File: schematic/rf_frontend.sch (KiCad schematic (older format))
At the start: 75 parts, among them J9 CONN_01X02, U10 Anaren_B0430J50100AHF, U11 MurataSF2314E, U12 MurataSF2314E, U13 SPF5043Z, U14 RFPA0133TR7, U15 MurataSF2314E, U16 RFSW1012, U17 MurataSF2314E, U8 SX1257, U9 SX1257

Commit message: Updates to schematic, components
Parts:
- C38, C45, C46, C47, C48, C49, C50, C51, C52, C53, C54, C55, C56, C57, C58, C60, C61, C62: footprint (none) -> Capacitors_SMD:C_0402
- C39, C40, C41, C42: value C -> 100nF; footprint (none) -> Capacitors_SMD:C_0402
- C43, C44: value C -> 10nF; footprint (none) -> Capacitors_SMD:C_0402
- C59, C66, C67: footprint 0603 -> Capacitors_SMD:C_0603
- C80: renamed from 1nF1; value C -> 100nF
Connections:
- wire segments 248 -> 249

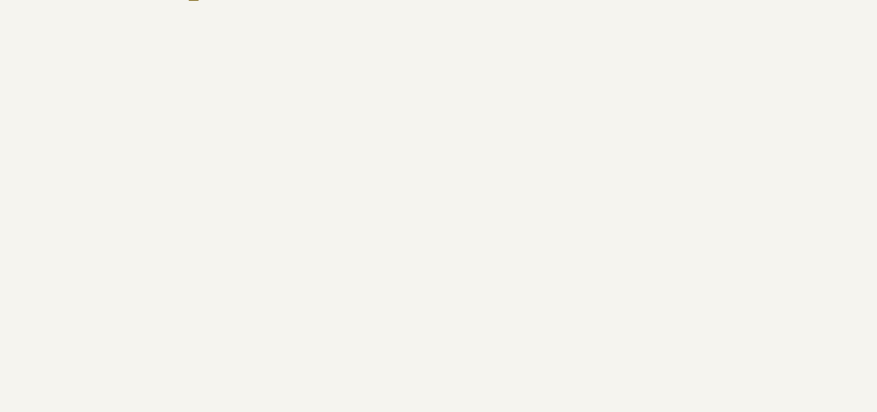
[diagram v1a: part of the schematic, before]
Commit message: Adds footprint for crystal
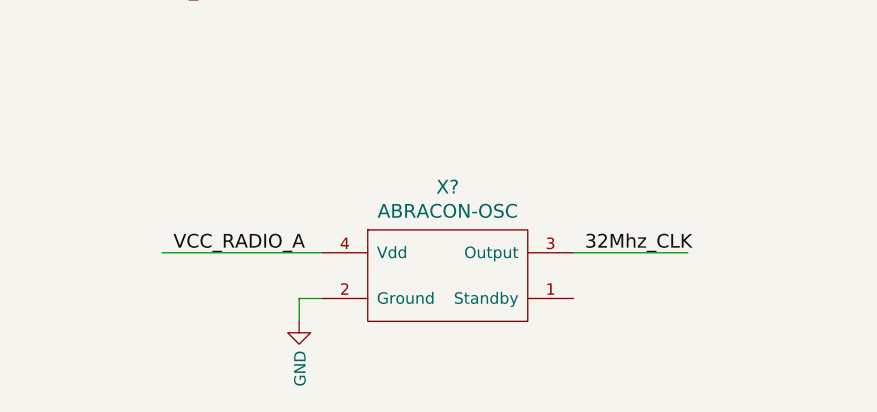
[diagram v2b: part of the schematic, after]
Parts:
- added X?: ABRACON-OSC, symbol ABRACON-OSC
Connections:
- wire segments 249 -> 253
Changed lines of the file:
@@
 Wire Wire Line
 	2300 4000 2300 3950
+$Comp
+L ABRACON-OSC X?
+U 1 1 59B585C5
+P 2800 10100
+F 0 "X?" H 2800 10487 60  0000 C CNN
+F 1 "ABRACON-OSC" H 2800 10381 60  0000 C CNN
+F 2 "" H 2800 10150 60  0001 C CNN
+F 3 "" H 2800 10150 60  0001 C CNN
+	1    2800 10100
+	1    0    0    -1
+$EndComp
+$Comp
+L GND #PWR?
+U 1 1 59B58D1B
+P 2150 10300
+F 0 "#PWR?" H 2150 10050 50  0001 C CNN
+F 1 "GND" V 2155 10172 50  0000 R CNN
+F 2 "" H 2150 10300 50  0001 C CNN
+F 3 "" H 2150 10300 50  0001 C CNN
+	1    2150 10300
+	1    0    0    -1
+$EndComp
+Wire Wire Line
+	2150 10300 2150 10200
+Wire Wire Line
+	2150 10200 2250 10200
+Wire Wire Line
+	1550 10000 2250 10000
+Text Label 1600 10000 0    60   ~ 0
+VCC_RADIO_A
+Wire Wire Line
+	3350 10000 3850 10000
+Text Label 3400 10000 0    60   ~ 0
+32Mhz_CLK
 $EndSCHEMATC

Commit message: Schematic capture almost done. RF layout started.
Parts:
- C34, C35, C63, C64, C65, C68, C69, C70, C71, C72, C73, C74, C75, C76, C77, C78, C80: footprint (none) -> Capacitors_SMD:C_0402
- J9: footprint (none) -> Connectors_Molex:Molex_SMA_Jack_Edge_Mount
- L2, L3, L4, L5, L8: footprint (none) -> Inductors_SMD:L_0402
- L6, L7: footprint (none) -> Inductors_SMD:L_0603
- R37, R38, R39, R40, R41, R42, R43, R44, R45, R46, R47, R48, R49: footprint (none) -> Resistors_SMD:R_0402
- U10: footprint (none) -> anaren_balun:anaren_balun
- U11, U12, U15, U17: footprint (none) -> murata_saw_filter:murata_saw_filter
- U13: footprint (none) -> quorvo:quorvo_spf5043z
- U14: footprint (none) -> Housings_DFN_QFN:QFN-16-1EP_3x3mm_Pitch0.5mm
- U16: footprint (none) -> quorvo:rfsw1012DS
- U8, U9: footprint (none) -> Housings_DFN_QFN:QFN-32-1EP_5x5mm_Pitch0.5mm
- X2: renamed from X?; footprint (none) -> crystal_osc_1:ABRACON-OSC
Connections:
- wire segments 253 -> 255

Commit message: RF layout updated. Rest still needs work
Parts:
- added C81: 1.5pF, Capacitors_SMD:C_0402_NoSilk, symbol C
- added R50: 30, Resistors_SMD:R_0402_NoSilk, symbol R
- C34, C35, C38, C39, C40, C41, C42, C43, C44, C45, C46, C47, C48, C49, C50, C51, C52, C53, C54, C56, C57, C58, C60, C61, C62, C63, C64, C65, C68, C69, C70, C71, C72, C73, C74, C75, C76, C77, C78, C80: footprint Capacitors_SMD:C_0402 -> Capacitors_SMD:C_0402_NoSilk
- C55: value 5.9pF -> 1.5pF; footprint Capacitors_SMD:C_0402 -> Capacitors_SMD:C_0402_NoSilk
- C59, C66, C67: footprint Capacitors_SMD:C_0603 -> Capacitors_SMD:C_0402_NoSilk
- J9: footprint Connectors_Molex:Molex_SMA_Jack_Edge_Mount -> Connectors:SMA_THT_Jack_Straight
- L2: value 33uH -> 1.5nH
- L3: value 3.9uH -> 1.5nH
- L6, L7: footprint Inductors_SMD:L_0603 -> Inductors_SMD:L_0402
- R37, R38, R39, R40, R41, R42, R43, R44, R45, R46, R47, R48, R49: footprint Resistors_SMD:R_0402 -> Resistors_SMD:R_0402_NoSilk
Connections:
- net labels removed: +3.3V, CLK_IN
- wire segments 255 -> 259
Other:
- moved on the sheet: C54

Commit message: Layout approaching final version. BOM updated
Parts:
- C38: footprint Capacitors_SMD:C_0402_NoSilk -> Capacitors_SMD:C_0603
- C63: value 0.1uF -> 100nF
- C64: value 10000pF -> 100nF
- C78: value 0.01uF -> 10nF
- C80: value 100nF -> 1nF; footprint Capacitors_SMD:C_0402_NoSilk -> Capacitors_SMD:C_0603
- L5: value L -> 100nH
- R48, R49: value 300 -> 100
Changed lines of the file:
@@
 P 9000 8200
 F 0 "L5" H 9053 8246 50  0000 L CNN
-F 1 "L" H 9053 8155 50  0000 L CNN
+F 1 "100nH" H 9053 8155 50  0000 L CNN
 F 2 "Inductors_SMD:L_0402" H 9000 8200 50  0001 C CNN
 F 3 "" H 9000 8200 50  0001 C CNN
@@
 P 9450 9150
 F 0 "C64" H 9335 9104 50  0000 R CNN
-F 1 "10000pF" H 9335 9195 50  0000 R CNN
+F 1 "100nF" H 9335 9195 50  0000 R CNN
 F 2 "Capacitors_SMD:C_0402_NoSilk" H 9488 9000 50  0001 C CNN
 F 3 "" H 9450 9150 50  0001 C CNN
@@
 P 14050 6050
 F 0 "C78" H 13935 6004 50  0000 R CNN
-F 1 "0.01uF" H 13935 6095 50  0000 R CNN
+F 1 "10nF" H 13935 6095 50  0000 R CNN
 F 2 "Capacitors_SMD:C_0402_NoSilk" H 14088 5900 50  0001 C CNN
 F 3 "" H 14050 6050 50  0001 C CNN
@@
 P 11100 2200
 F 0 "R48" V 10893 2200 50  0000 C CNN
-F 1 "300" V 10984 2200 50  0000 C CNN
+F 1 "100" V 10984 2200 50  0000 C CNN
 F 2 "Resistors_SMD:R_0402_NoSilk" V 11030 2200 50  0001 C CNN
 F 3 "" H 11100 2200 50  0001 C CNN
@@
 P 9400 5000
 F 0 "C63" H 9515 5046 50  0000 L CNN
-F 1 "0.1uF" H 9515 4955 50  0000 L CNN
+F 1 "100nF" H 9515 4955 50  0000 L CNN
 F 2 "Capacitors_SMD:C_0402_NoSilk" H 9438 4850 50  0001 C CNN
 F 3 "" H 9400 5000 50  0001 C CNN
@@
 P 11550 2800
 F 0 "R49" V 11343 2800 50  0000 C CNN
-F 1 "300" V 11434 2800 50  0000 C CNN
+F 1 "100" V 11434 2800 50  0000 C CNN
 F 2 "Resistors_SMD:R_0402_NoSilk" V 11480 2800 50  0001 C CNN
 F 3 "" H 11550 2800 50  0001 C CNN
@@
 F 0 "C38" H 2265 2646 50  0000 L CNN
 F 1 "1nF" H 2265 2555 50  0000 L CNN
-F 2 "Capacitors_SMD:C_0402_NoSilk" H 2188 2450 50  0001 C CNN
+F 2 "Capacitors_SMD:C_0603" H 2188 2450 50  0001 C CNN
 F 3 "" H 2150 2600 50  0001 C CNN
 	1    2150 2600
@@
 P 2000 6300
 F 0 "C80" H 2115 6346 50  0000 L CNN
-F 1 "100nF" H 2115 6255 50  0000 L CNN
-F 2 "Capacitors_SMD:C_0402_NoSilk" H 2038 6150 50  0001 C CNN
+F 1 "1nF" H 2115 6255 50  0000 L CNN
+F 2 "Capacitors_SMD:C_0603" H 2038 6150 50  0001 C CNN
 F 3 "" H 2000 6300 50  0001 C CNN
 	1    2000 6300
